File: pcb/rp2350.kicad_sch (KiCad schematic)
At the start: 31 parts, among them SW1 BOOTSEL, SW2 RESET, U1 RP2350_60QFN, U4 W25Q16JVZPIQ, Y1 Crystal_GND24

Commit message: nfc and battery charge stuff
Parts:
- Y1: value Crystal_GND24 -> ABM8-272-T3

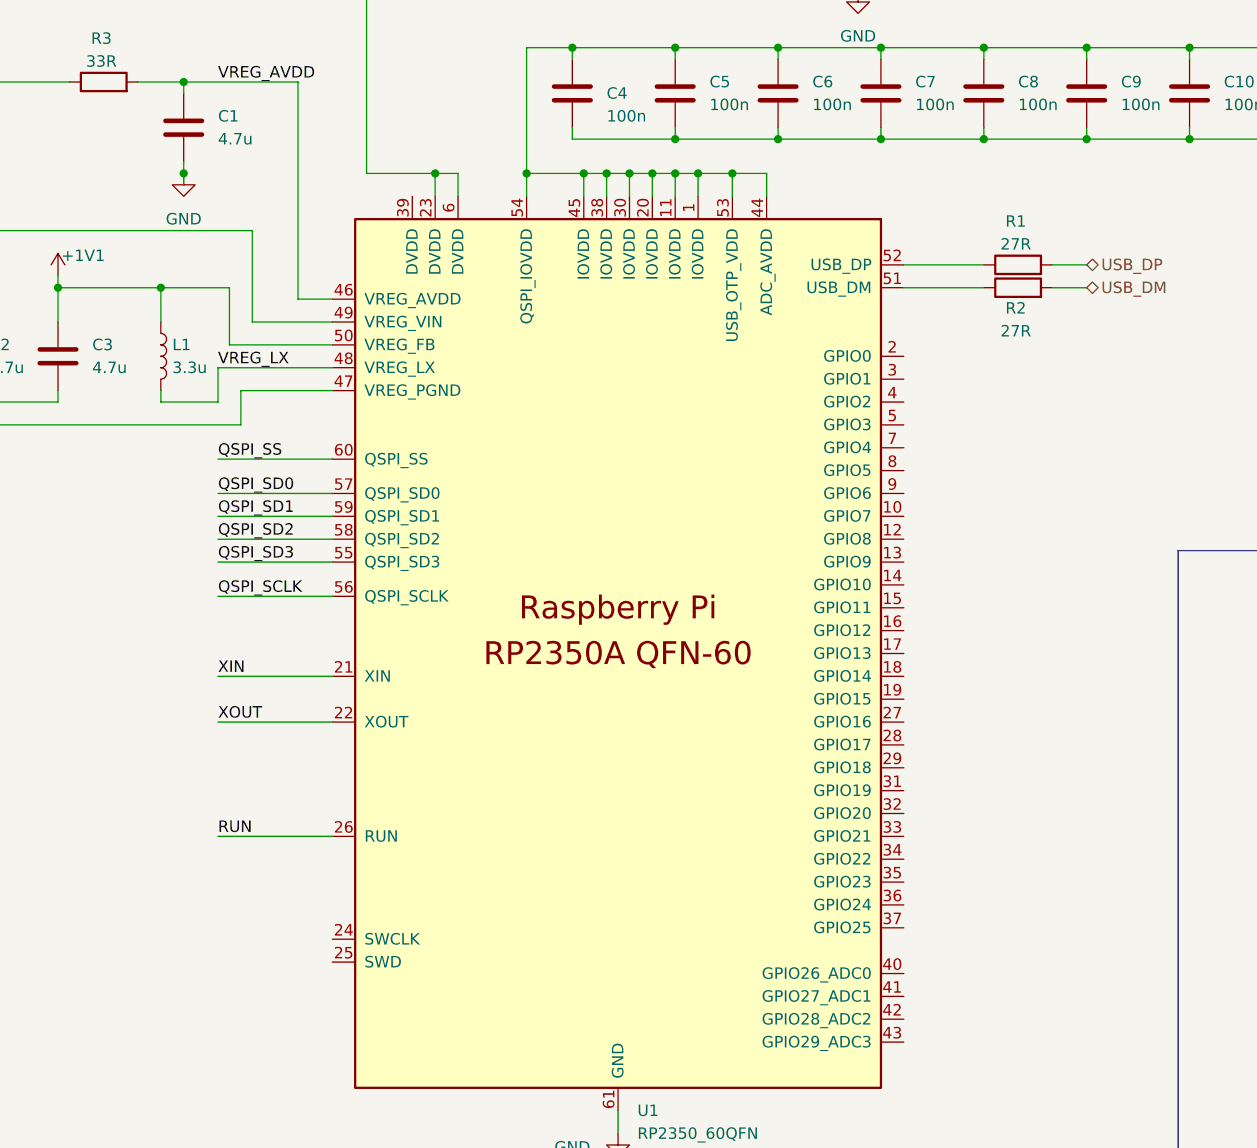
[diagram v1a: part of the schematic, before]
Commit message: nfc tuning, new charger IC
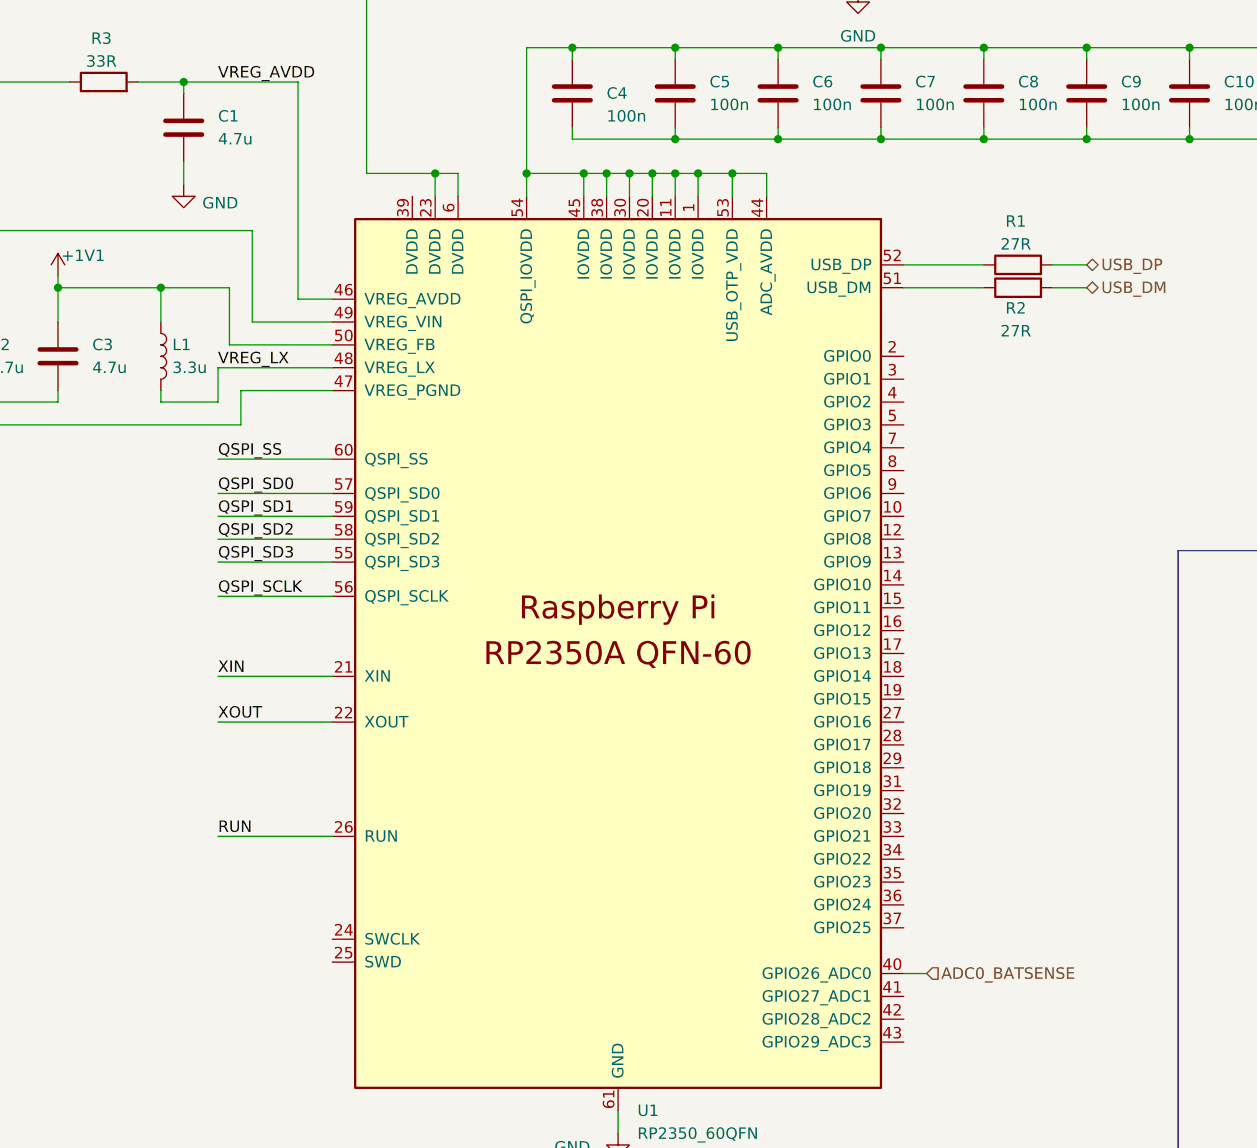
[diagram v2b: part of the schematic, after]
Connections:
- net ADC0_BATSENSE: now reaches U1.40 (GPIO26_ADC0)
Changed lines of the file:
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@@
 	)
 	(junction
-		(at 95.25 52.07)
-		(diameter 0)
-		(color 0 0 0 0)
-	)
-	(junction
 		(at 236.22 132.08)
 		(diameter 0)
@@
 	(wire
 		(pts
-			(xy 95.25 53.34) (xy 95.25 52.07)
-		)
-		(stroke
-			(width 0)
-			(type default)
-		)
-	)
-	(wire
-		(pts
 			(xy 195.58 48.26) (xy 207.01 48.26)
 		)
@@
 	(wire
 		(pts
+			(xy 95.25 50.8) (xy 95.25 53.34)
+		)
+		(stroke
+			(width 0)
+			(type default)
+		)
+	)
+	(wire
+		(pts
 			(xy 69.85 76.2) (xy 69.85 77.47)
 		)
@@
 	(wire
 		(pts
+			(xy 175.26 140.97) (xy 177.8 140.97)
+		)
+		(stroke
+			(width 0)
+			(type default)
+		)
+	)
+	(wire
+		(pts
 			(xy 161.29 30.48) (xy 170.18 30.48)
 		)
@@
 	(wire
 		(pts
-			(xy 95.25 50.8) (xy 95.25 52.07)
-		)
-		(stroke
-			(width 0)
-			(type default)
-		)
-	)
-	(wire
-		(pts
 			(xy 99.06 92.71) (xy 111.76 92.71)
 		)
@@
 		)
 	)
+	(hierarchical_label "ADC0_BATSENSE"
+		(shape input)
+		(at 177.8 140.97 0)
+		(effects
+			(font
+				(size 1.27 1.27)
+			)
+			(justify left)
+		)
+	)
 	(hierarchical_label "USB_DM"
 		(shape bidirectional)
@@
 	(symbol
 		(lib_id "power:GND")
-		(at 95.25 52.07 0)
-		(unit 1)
-		(exclude_from_sim no)
-		(in_bom yes)
-		(on_board yes)
-		(dnp no)
-		(fields_autoplaced yes)
-		(property "Reference" "#PWR02"
-			(at 95.25 58.42 0)
-			(effects
-				(font
-					(size 1.27 1.27)
-				)
-				(hide yes)
-			)
-		)
-		(property "Value" "GND"
-			(at 95.25 57.15 0)
-			(effects
-				(font
-					(size 1.27 1.27)
-				)
-			)
-		)
-		(property "Footprint" ""
-			(at 95.25 52.07 0)
-			(effects
-				(font
-					(size 1.27 1.27)
-				)
-				(hide yes)
-			)
-		)
-		(property "Datasheet" ""
-			(at 95.25 52.07 0)
-			(effects
-				(font
-					(size 1.27 1.27)
-				)
-				(hide yes)
-			)
-		)
-		(property "Description" "Power symbol creates a global label with name \"GND\" , ground"
-			(at 95.25 52.07 0)
-			(effects
-				(font
-					(size 1.27 1.27)
-				)
-				(hide yes)
-			)
-		)
-		(pin "1"
-		)
-		(instances
-			(project ""
-				(path "/21842aa8-f461-4adb-8a2d-bf0920423cff/30df8f44-7ac0-4504-aa3a-cfe85e0767a2"
-					(reference "#PWR02")
-					(unit 1)
-				)
-			)
-		)
-	)
-	(symbol
-		(lib_id "power:GND")
 		(at 69.85 82.55 0)
 		(unit 1)
@@
 					(unit 1)
 				)
+			)
+		)
+	)
+	(symbol
+		(lib_id "power:GND")
+		(at 95.25 53.34 0)
+		(unit 1)
+		(exclude_from_sim no)
+		(in_bom yes)
+		(on_board yes)
+		(dnp no)
+		(property "Reference" "#PWR02"
+			(at 95.25 59.69 0)
+			(effects
+				(font
+					(size 1.27 1.27)
+				)
+				(hide yes)
+			)
+		)
+		(property "Value" "GND"
+			(at 99.314 55.372 0)
+			(effects
+				(font
+					(size 1.27 1.27)
+				)
+			)
+		)
+		(property "Footprint" ""
+			(at 95.25 53.34 0)
+			(effects
+				(font
+					(size 1.27 1.27)
+				)
+				(hide yes)
+			)
+		)
+		(property "Datasheet" ""
+			(at 95.25 53.34 0)
+			(effects
+				(font
+					(size 1.27 1.27)
+				)
+				(hide yes)
+			)
+		)
+		(property "Description" "Power symbol creates a global label with name \"GND\" , ground"
+			(at 95.25 53.34 0)
+			(effects
+				(font
+					(size 1.27 1.27)
+				)
+				(hide yes)
+			)
+		)
+		(pin "1"
+		)
+		(instances
+			(project "flopperone"
+				(path "/21842aa8-f461-4adb-8a2d-bf0920423cff/30df8f44-7ac0-4504-aa3a-cfe85e0767a2"
+					(reference "#PWR02")
+					(unit 1)
+				)
